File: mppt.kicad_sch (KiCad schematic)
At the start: 49 parts, among them J10 Fan_F, J9 Fan_M, M1 Fan_3pin, Q1 IPP019N08NF2S, Q2 IPP019N08NF2S, Q3 IPP019N08NF2S, Q4 Si2306BDS, Q5 Si2306BDS, U2 ACS758xCB, U3 L6398D, U4 TME 1212S, U5 ACS758xCB

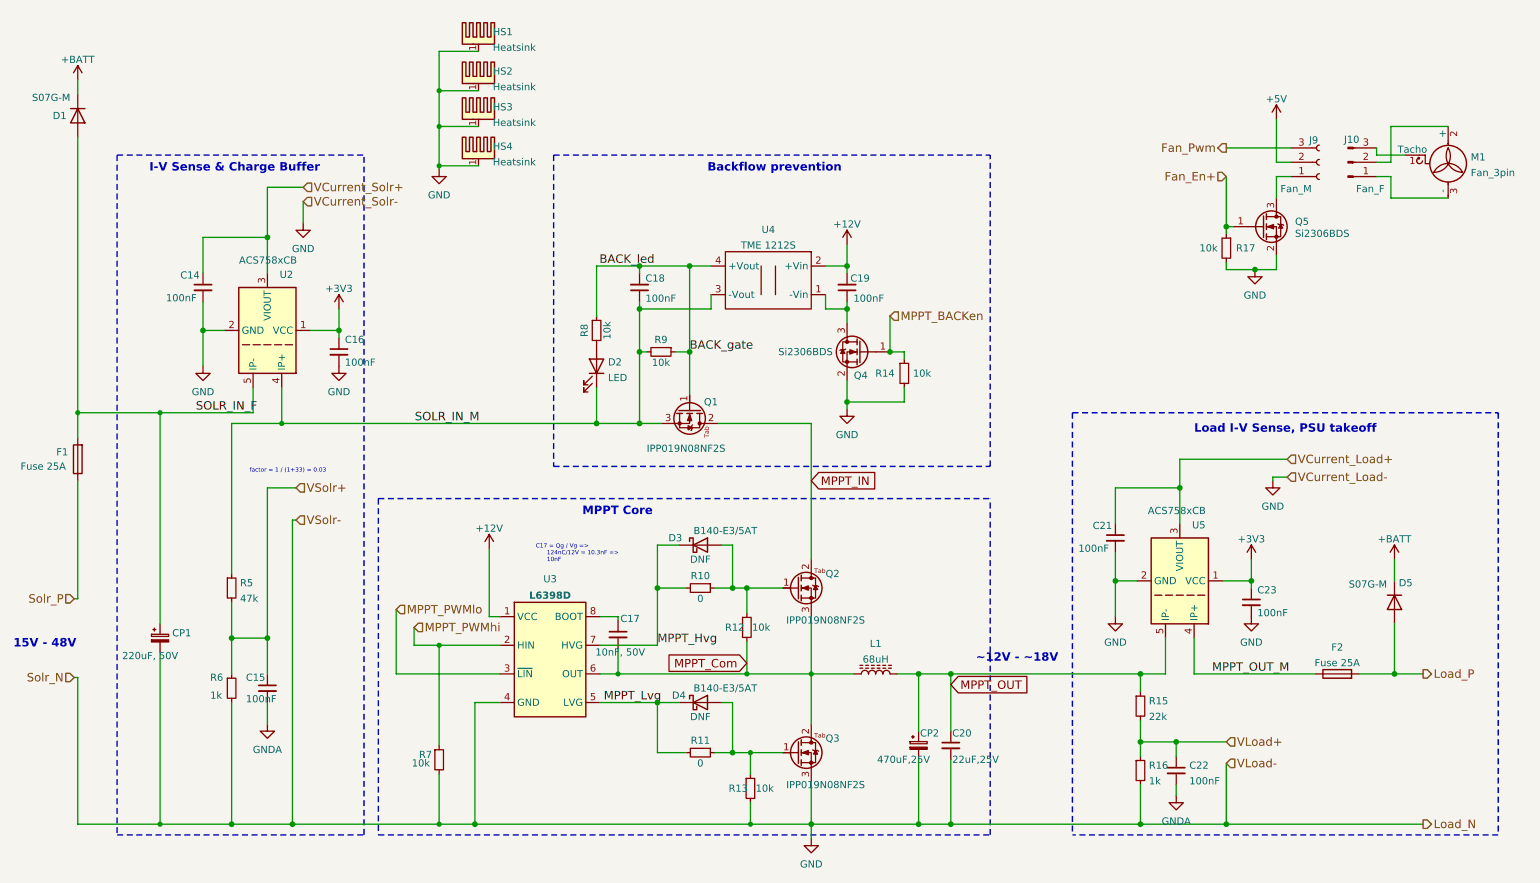
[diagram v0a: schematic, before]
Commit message: Update for Kicad 6-rc; replace 12V reg and cascade; add EEPROM;
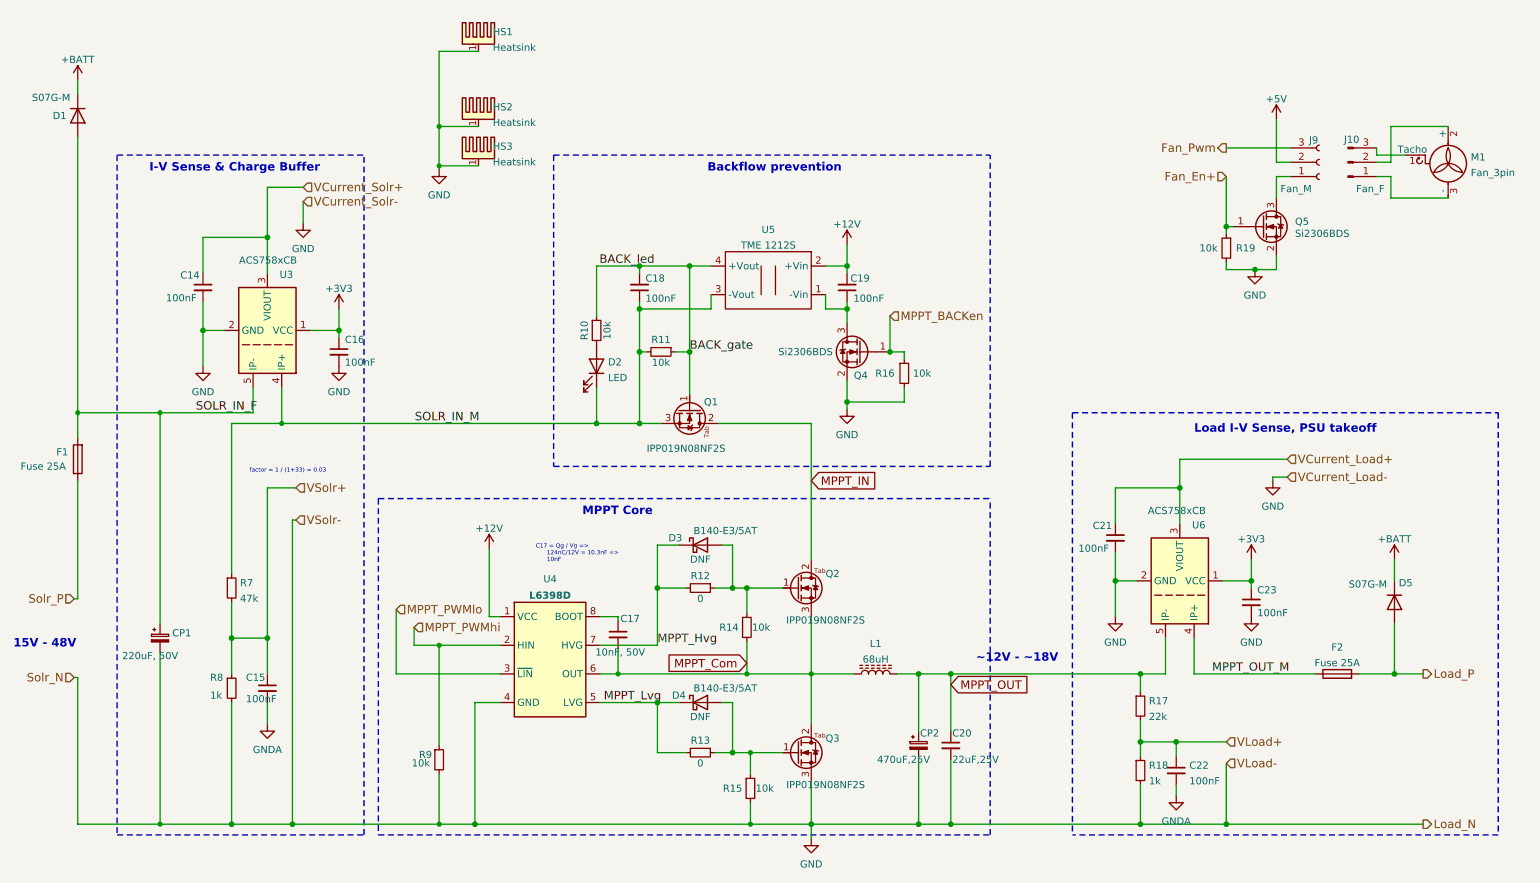
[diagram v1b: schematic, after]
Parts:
- removed HS2: Heatsink, MountingHole:MountingHole_2.2mm_M2_Pad_Via, symbol Mechanical:Heatsink_Pad
- Q1, Q2, Q3: footprint Package_TO_SOT_THT:TO-220-3_Vertical -> solarpump:TO-220-3_StaggeredB_Vertical
- renumbered HS3 to HS2, HS4 to HS3, R8 to R10, R9 to R11, R10 to R12, R11 to R13, R12 to R14, R13 to R15, R14 to R16, R15 to R17, R16 to R18, R17 to R19, R5 to R7, R6 to R8, R7 to R9, U2 to U3, U3 to U4, U4 to U5, U5 to U6

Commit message: Fix diode FP errors, add models; link in regulator error sig; add new coil 3d model; lots of small tweaks
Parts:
- D1, D5: footprint Diode_SMD:D_SOD-123 -> Diode_SMD:D_SMF
- D3, D4: footprint Diode_SMD:D_SOD-123 -> Diode_SMD:D_SMA
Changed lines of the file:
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@@
       (effects (font (size 1.27 1.27)) (justify left))
     )
-    (property "Footprint" "Diode_SMD:D_SOD-123" (id 2) (at 253.365 120.015 0)
+    (property "Footprint" "Diode_SMD:D_SMF" (id 2) (at 253.365 120.015 0)
       (effects (font (size 1.27 1.27)) hide)
     )
@@
     (property "Reference" "D3" (id 0) (at 130.175 108.585 0))
     (property "Value" "B140-E3/5AT" (id 1) (at 139.065 107.315 0))
-    (property "Footprint" "Diode_SMD:D_SOD-123" (id 2) (at 134.62 109.855 0)
+    (property "Footprint" "Diode_SMD:D_SMA" (id 2) (at 134.62 109.855 0)
       (effects (font (size 1.27 1.27)) hide)
     )
@@
       (effects (font (size 1.27 1.27)) (justify left))
     )
-    (property "Footprint" "Diode_SMD:D_SOD-123" (id 2) (at 19.685 33.655 0)
+    (property "Footprint" "Diode_SMD:D_SMF" (id 2) (at 19.685 33.655 0)
       (effects (font (size 1.27 1.27)) hide)
     )
@@
     (property "Reference" "D4" (id 0) (at 130.81 136.525 0))
     (property "Value" "B140-E3/5AT" (id 1) (at 139.065 135.255 0))
-    (property "Footprint" "Diode_SMD:D_SOD-123" (id 2) (at 134.62 137.795 0)
-      (effects (font (size 1.27 1.27)) hide)
-    )
+    (property "Footprint" "Diode_SMD:D_SMA" (id 2) (at 134.62 137.795 0)
+      (effects (font (size 1.27 1.27)) hide)
+    )

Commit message: Various important tweaks and fixes.
Fix several incorrect capacitor footprints;
Fix slightly incorrect footprint for USB connector;
Add ground vias around MPPT circuit;
Add Zener protection circuit for regulation error input;
Use pin header not socket for Pico Display header;
Fix missing connection to featherwing i2c;
Add in 3d models for USB socket and switch
Update kicad sheet dates;
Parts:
- CP2: footprint Capacitor_THT:C_Radial_D10.0mm_H16.0mm_P5.00mm -> Capacitor_THT:CP_Radial_D8.0mm_P3.50mm
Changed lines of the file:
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@@
   (title_block
     (title "SolarPump v3")
-    (date "2021-11-15")
+    (date "2021-12-03")
     (rev "1.0")
     (company "IvimeyCom")
@@
       (effects (font (size 1.27 1.27)) (justify left))
     )
-    (property "Footprint" "Capacitor_THT:C_Radial_D10.0mm_H16.0mm_P5.00mm" (id 2) (at 173.355 145.415 0)
-      (effects (font (size 1.27 1.27)) hide)
-    )
+    (property "Footprint" "Capacitor_THT:CP_Radial_D8.0mm_P3.50mm" (id 2) (at 173.355 145.415 0)
+      (effects (font (size 1.27 1.27)) hide)
+    )

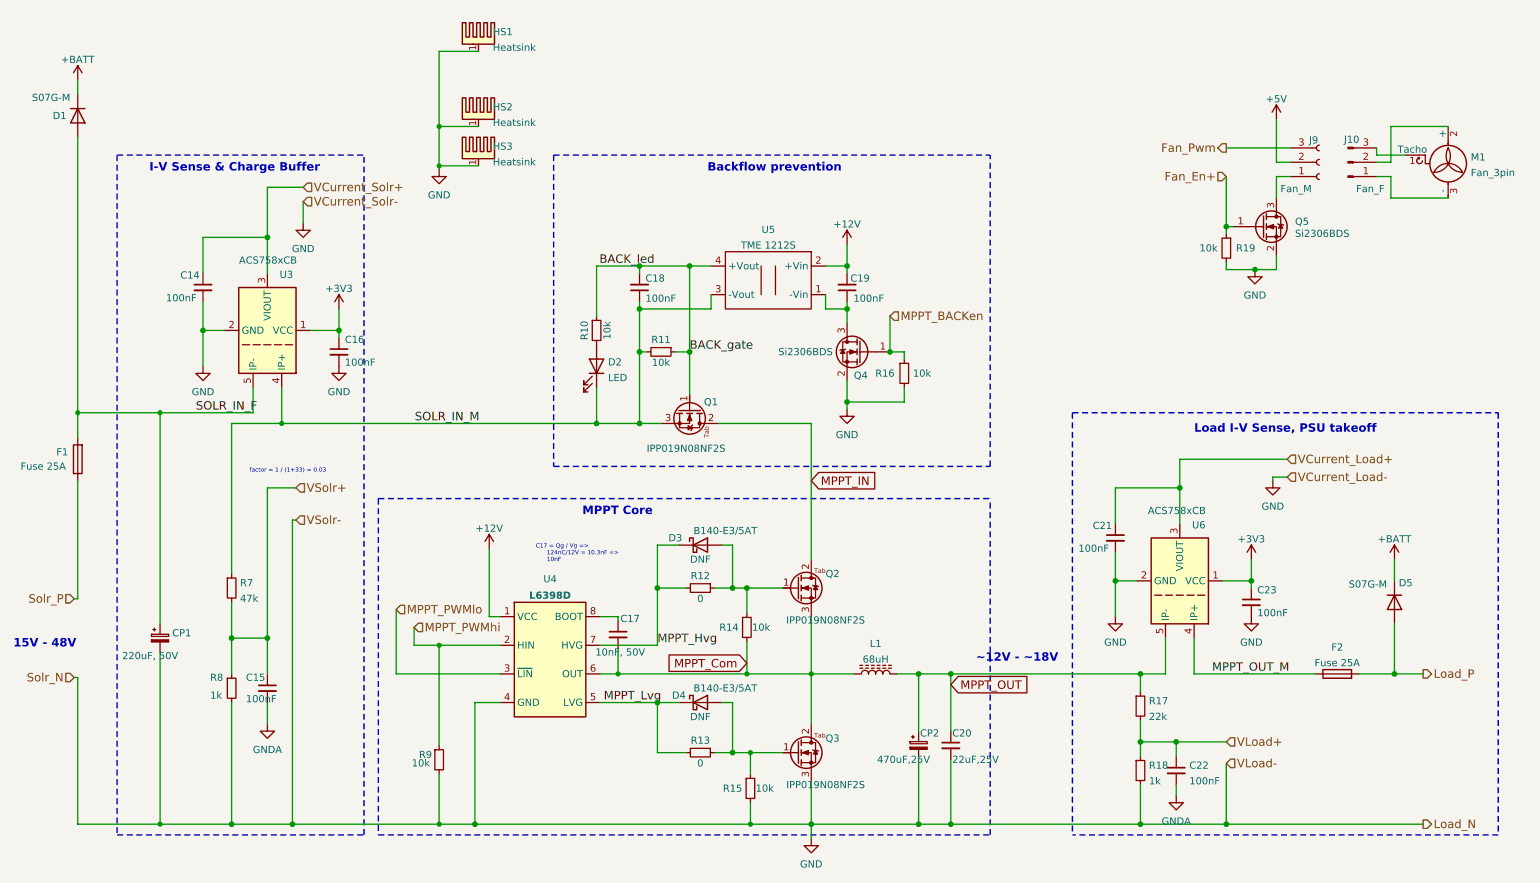
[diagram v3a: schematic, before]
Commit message: Rework with larger display; update component selection; add SWD conn; add RTC chip and QWIIC i2c socket
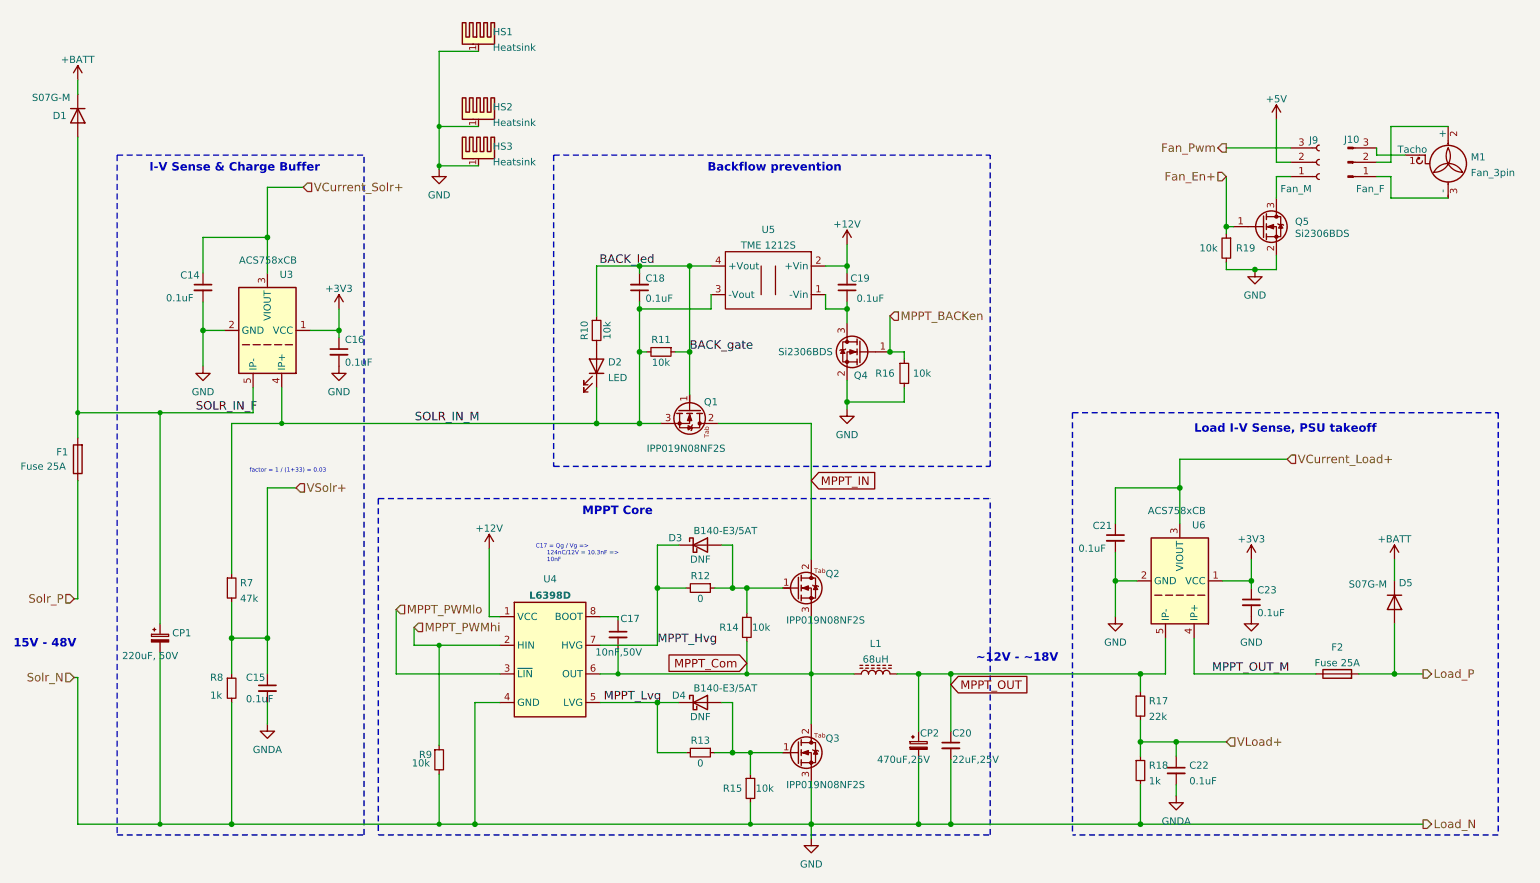
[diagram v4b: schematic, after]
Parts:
- C14, C15, C16, C18, C19, C21, C22, C23: value 100nF -> 0.1uF; Mfr KEMET -> Samsung Electro-Mechanics; Mfr Part No C0402C104K8R7411 -> CL21B104KACNNND; Supl Part No 80-C0402C104K8R7411 -> 187-CL21B104KACNNND
- C17: value 10nF, 50V -> 10nF,50V; Mfr Samsung Electro-Mechanics -> KEMET; Mfr Part No (none) -> C0805C103J5R; Supl Part No (none) -> 80-C0805C103J5R; Supl Price 0.07 -> 0.077
- C20: Mfr Samsung -> Samsung Electro-Mechanics; Mfr Part No CL32A226KAJNNNE -> CL21A226MAQNNNE; Supl Part No 187-CL32A226KAJNNNE -> 187-CL21A226MAQNNNE; Supl Price 0.411 -> 0.25

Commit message: More updates to regularise property names
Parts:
- C14, C15, C16, C18, C19, C21, C22, C23: Manuf (none) -> Samsung Electro-Mechanics; Mfr Samsung Electro-Mechanics -> (none); Mfr Part No CL21B104KACNNND -> (none); Part (none) -> CL21B104KACNNND; Supl Mouser -> (none); Supl Part No 187-CL21B104KACNNND -> (none); Supl Price 0.016 -> (none); Vendor (none) -> Mouser; Vendor Cost (none) -> 0.016; Vendor SKU (none) -> 187-CL21B104KACNNND
- C17: Manuf (none) -> KEMET; Mfr KEMET -> (none); Mfr Part No C0805C103J5R -> (none); Part (none) -> C0805C103J5R; Supl Mouser -> (none); Supl Part No 80-C0805C103J5R -> (none); Supl Price 0.077 -> (none); Suppl Mouser -> (none); Vendor (none) -> Mouser; Vendor Cost (none) -> 0.077; Vendor SKU (none) -> 80-C0805C103J5R
- C20: Manuf (none) -> Samsung Electro-Mechanics; Mfr Samsung Electro-Mechanics -> (none); Mfr Part No CL21A226MAQNNNE -> (none); Part (none) -> CL21A226MAQNNNE; Supl Mouser -> (none); Supl Part No 187-CL21A226MAQNNNE -> (none); Supl Price 0.25 -> (none); Vendor (none) -> Mouser; Vendor Cost (none) -> 0.25; Vendor SKU (none) -> 187-CL21A226MAQNNNE
- CP1: Manuf (none) -> Nichicon; Mfr Nichicon -> (none); Mfr Part No UPM1H221MHD6TD -> (none); Part (none) -> UPM1H221MHD6TD; Supl Mouser -> (none); Supl Part No 647-UPM1H221MHD6TD -> (none); Supl Price 0.587 -> (none); Vendor (none) -> Mouser; Vendor Cost (none) -> 0.587; Vendor SKU (none) -> 647-UPM1H221MHD6TD
- CP2: Manuf (none) -> KEMET; Mfr KEMET -> (none); Mfr Part No ESW477M025AH2AA -> (none); Part (none) -> ESW477M025AH2AA; Supl Mouser -> (none); Supl Part No 80-ESW477M025AH2AA -> (none); Supl Price 0.382 -> (none); Vendor (none) -> Mouser; Vendor Cost (none) -> 0.382; Vendor SKU (none) -> 80-ESW477M025AH2AA
- D1, D5: Manuf (none) -> Vishay; Mfr Vishay -> (none); Mfr Part No S07G-M -> (none); Part (none) -> S07G-M; Supl Mouser -> (none); Supl Part No 78-S07G-M-18 -> (none); Supl Price 0.29 -> (none); Vendor (none) -> Mouser; Vendor Cost (none) -> 0.29; Vendor SKU (none) -> 78-S07G-M-18
- D2: Manuf (none) -> Wurth Elektronik; Mfr Wurth Elektronik -> (none); Mfr Part No 150080YS75000 -> (none); Part (none) -> 150080YS75000; Supl Mouser -> (none); Supl Part No 710-150080YS75000 -> (none); Supl Price 0.137 -> (none); Vendor (none) -> Mouser; Vendor Cost (none) -> 0.137; Vendor SKU (none) -> 710-150080YS75000
- D3, D4: value B140-E3/5AT -> B140-E3; Manuf (none) -> Vishay; Mfr Vishay -> (none); Mfr Part No B140-E3 -> (none); Part (none) -> B140-E3/5AT; Supl Mouser -> (none); Supl Part No 625-B140-E3 -> (none); Supl Price 0.277 -> (none); Vendor (none) -> Mouser; Vendor Cost (none) -> 0.277; Vendor SKU (none) -> 625-B140-E3
- F1, F2: Manuf (none) -> Keystone; Mfr Keystone -> (none); Mfr Part No 3555-2 -> (none); Part (none) -> 3555-2; Supl Mouser -> (none); Supl Part No 534-3555-2 -> (none); Supl Price 1.46 -> (none); Vendor (none) -> Mouser; Vendor Cost (none) -> 1.46; Vendor SKU (none) -> 534-3555-2
- J9: Manuf (none) -> Molex; Mfr Molex -> (none); Mfr Part No 171856-0003 -> (none); Part (none) -> 171856-0003; Supl Mouser -> (none); Supl Part No 538-171856-0003 -> (none); Supl Price 0.26 -> (none); Vendor (none) -> Mouser; Vendor Cost (none) -> 0.26; Vendor SKU (none) -> 538-171856-0003
- Q1, Q2, Q3: Manuf (none) -> Infineon / IR; Mfr Infineon / IR -> (none); Mfr Part No IPP019N08NF2S -> (none); Part (none) -> IPP019N08NF2S; Supl Mouser -> (none); Supl Part No 942-IPP019N08NF2S -> (none); Supl Price 2.55 -> (none); Vendor (none) -> Mouser; Vendor Cost (none) -> 2.55; Vendor SKU (none) -> 942-IPP019N08NF2S
- Q4, Q5: Manuf (none) -> Vishay; Mfr Vishay -> (none); Mfr Part No SI2306BDS-T1-E3 -> (none); Part (none) -> SI2306BDS-T1-E3; Supl Mouser -> (none); Supl Part No 781-SI2306BDS-E3 -> (none); Supl Price 0.496 -> (none); Vendor (none) -> Mouser; Vendor Cost (none) -> 0.496; Vendor SKU (none) -> 781-SI2306BDS-E3
- R10, R11, R14, R15, R16, R19, R9: Manuf (none) -> Yageo; Mfr Yageo -> (none); Mfr Part No AC0805FR-0710KL -> (none); Part (none) -> AC0805FR-0710KL; Supl Mouser -> (none); Supl Part No 603-AC0805FR-0710KL -> (none); Supl Price 0.077 -> (none); Vendor (none) -> Mouser; Vendor Cost (none) -> 0.077; Vendor SKU (none) -> 603-AC0805FR-0710KL
- R12, R13: Manuf (none) -> Yageo; Mfr Yageo -> (none); Mfr Part No RC0805FR-070RL -> (none); Part (none) -> RC0805FR-070RL; Supl Mouser -> (none); Supl Part No 603-RC0805FR-070RL -> (none); Supl Price 0.077 -> (none); Vendor (none) -> Mouser; Vendor Cost (none) -> 0.077; Vendor SKU (none) -> 603-RC0805FR-070RL
- R17: Manuf (none) -> Yageo; Mfr Yageo -> (none); Mfr Part No RC0805FR-0722KL -> (none); Part (none) -> RC0805FR-0722KL; Supl Mouser -> (none); Supl Part No 603-RC0805FR-0722KL -> (none); Supl Price 0.077 -> (none); Vendor (none) -> Mouser; Vendor Cost (none) -> 0.077; Vendor SKU (none) -> 603-RC0805FR-0722KL
- R18, R8: Manuf (none) -> Yageo; Mfr Yageo -> (none); Mfr Part No RC0805FR-071KL -> (none); Part (none) -> RC0805FR-071KL; Supl Mouser -> (none); Supl Part No 603-RC0805FR-071KL -> (none); Supl Price 0.077 -> (none); Vendor (none) -> Mouser; Vendor Cost (none) -> 0.077; Vendor SKU (none) -> 603-RC0805FR-071KL
- R7: Manuf (none) -> Bourns; Mfr Bourns -> (none); Mfr Part No CR0805FX-4702ELF -> (none); Part (none) -> CR0805FX-4702ELF; Supl Mouser -> (none); Supl Part No 652-CR0805FX-4702ELF -> (none); Supl Price 0.077 -> (none); Vendor (none) -> Mouser; Vendor Cost (none) -> 0.077; Vendor SKU (none) -> 652-CR0805FX-4702ELF
- U4: Manuf (none) -> STMicroelectronics; Mfr STMicroelectronics -> (none); Mfr Part No L6398D -> (none); Part (none) -> L6398D; Supl Mouser -> (none); Supl Part No 511-L6398D -> (none); Supl Price 1.32 -> (none); Vendor (none) -> Mouser; Vendor Cost (none) -> 1.32; Vendor SKU (none) -> 511-L6398D
- U5: Manuf (none) -> TRACO Power; Mfr TRACO Power -> (none); Mfr Part No TME-1212S -> (none); Part (none) -> TME-1212S; Supl Mouser -> (none); Supl Part No 495-TME-1212S -> (none); Supl Price 3.85 -> (none); Vendor (none) -> Mouser; Vendor Cost (none) -> 3.85; Vendor SKU (none) -> 495-TME-1212S
